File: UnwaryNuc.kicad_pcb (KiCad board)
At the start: 4 copper layers, 125.3 x 66.8 mm, 182 parts, among them J1 USB_B_Micro, J10 Conn_01x10_Male, J2 USB_A_Dual, J3 Conn_01x06_Male, J4 RJ45_Amphenol_RJMG1BD3B8K1ANR, J5 RJ45_Amphenol_RJMG1BD3B8K1ANR, J6 Conn_02x04_Odd_Even, J7 Conn_02x04_Odd_Even, J8 Conn_02x04_Odd_Even, J9 Conn_01x04_Male, Q1 2N3904, Q2 BC856BDW1, SW1 SW_SPST, U1 NUC980DF71YC, U2 LAN8740A-EN-TR, U3 LAN8740A-EN-TR, U4 LD3985M18R_TSOT23, U5 MIC4690, U6 LM3880, U7 AP2127K-1.2, U8 S25FL127SABMFV100, X1 ASE-xxxMHz, X2 ASE-xxxMHz, Y1 ABS07-166, Y2 NX5032GA

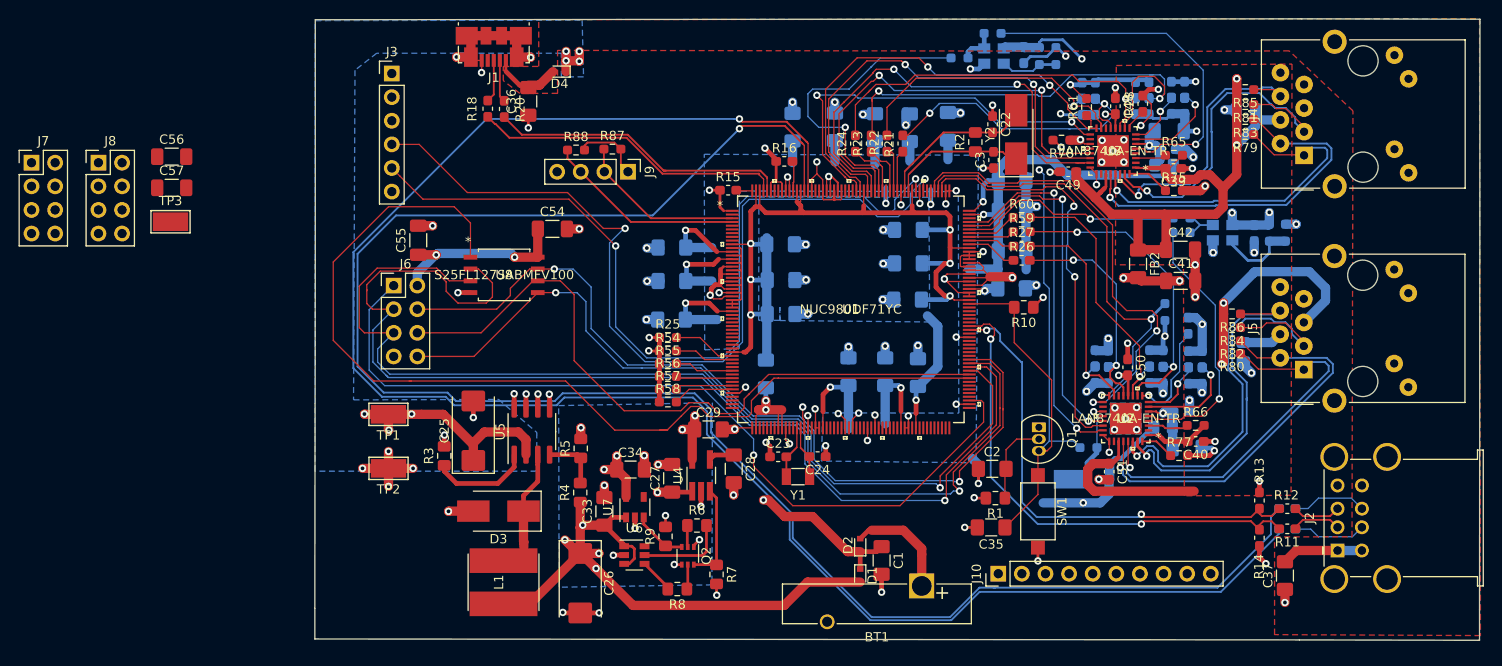
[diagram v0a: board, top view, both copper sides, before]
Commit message: routed SPI0 and SPI1, cleaned up top silk, added some random mounting holes.
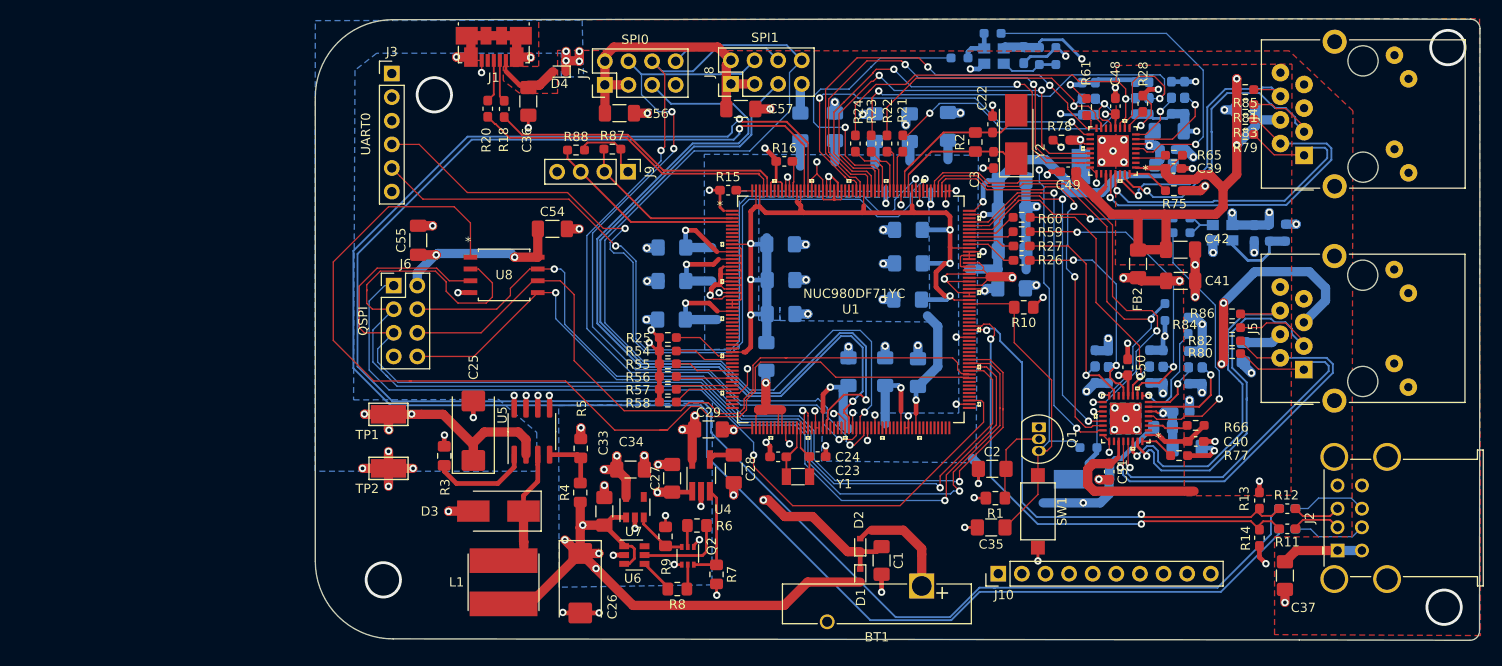
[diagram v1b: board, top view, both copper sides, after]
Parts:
- TP3: moved to B.Cu
- moved TP3 98.1 mm to (165.0, 75.6), turned to 90 degrees
- moved J8 68.6 mm to (127.4, 66.8), turned to 90 degrees
- moved J7 62.2 mm to (113.8, 66.9), turned to 90 degrees
- moved C57 61.8 mm to (128.5, 69.4)
- moved C56 48.4 mm to (115.4, 69.9)
- moved FB1 1.88 mm to (131.2, 96.1)
- moved C14 0.84 mm to (134.9, 71.4)
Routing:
- net /SPI0_MOSI: track 0.00 -> 100.1 mm, vias 0 -> 1
- net /SPIO_SS0: track 0.00 -> 88.1 mm, vias 0 -> 1
- net /SPI0_MISO: track 0.00 -> 84.6 mm, vias 0 -> 3
- net /SPI0_SS1: track 0.00 -> 84.1 mm, vias 0 -> 1
- net /SPI0_CLK: track 0.00 -> 84.1 mm, vias 0 -> 2
- net +3V3: track 365.9 -> 405.7 mm
- net GND: track 270.9 -> 279.2 mm
- net /QSPI0_CLK: track 75.0 -> 78.5 mm
- net +1V2: track 280.0 -> 283.2 mm
- net /P0_nRST: track 2.31 -> 5.23 mm
- net /QSPI0_SS0: track 107.5 -> 110.3 mm
- net +3.3VA: track 11.3 -> 13.2 mm, vias 2 -> 1
- net /USB1_P: track 191.9 -> 190.0 mm
- net /RMII0_REFCLK: track 33.6 -> 32.6 mm
- net /UART0_TXD: track 89.8 -> 88.9 mm
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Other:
- outline, holes or cut-outs redrawn
- board text added: "QSPI"
- board text added: "SPI0"
- board text added: "SPI1"
- board text added: "UART0"

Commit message: Routed some of PB row, 5 to go.
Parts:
- moved R58 3.54 mm to (117.1, 100.7), turned to 180 degrees
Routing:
- net /PB6: track 0.00 -> 156.3 mm, vias 0 -> 3
- net /PB4: track 0.00 -> 145.3 mm, vias 0 -> 3
- net /PB0: track 0.00 -> 143.6 mm, vias 0 -> 3
- net /USB1_N: track 192.1 -> 184.3 mm
- net /USB1_P: track 190.0 -> 183.2 mm
- net /BTSEL1: track 6.58 -> 12.5 mm
- net /QSPI0_CLK: track 78.5 -> 83.0 mm
- net /QSPI0_SS1: track 91.9 -> 90.6 mm
- net GND: track 279.2 -> 279.8 mm
- net /SPI0_MISO: track 84.6 -> 84.1 mm

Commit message: finished, board as produced
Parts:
- moved C28 0.15 mm to (127.6, 108.2)
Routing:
- net /PB7: track 0.00 -> 61.8 mm
- net /PB5: track 0.00 -> 56.4 mm
- net /PB3: track 0.00 -> 49.2 mm
- net /PB1: track 0.00 -> 45.2 mm
- net /PB2: track 0.00 -> 43.3 mm
- net +3.3VA: track 13.2 -> 49.1 mm
- net /VDD_RTC: track 26.8 -> 28.6 mm
- net /QSPI0_SS1: track 90.6 -> 89.6 mm
- net Net-(BT1-Pad1): track 11.8 -> 10.9 mm
